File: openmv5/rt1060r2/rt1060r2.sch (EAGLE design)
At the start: 244 parts, among them CN1 S2B-PH-K-S(LF)(SN), IC1 LM66200DRLR, IC2 TCR2LF33,LM_CT, IC3 AP61300Z6-7, IC4 IS42S16160G-6BL, IC5 IS25LP128F-JKLE-TR, IC6 ATECC608B-MAHDA-T, IC7 MXC4005XC, IC8 KSZ8081RNDCA-TR, IC9 MIMXRT1052DVL6B, J1 USB4105-GF-A, J2 USD-1040310811, J3 DF12-36-DS, J4 DNP, J5 DNP, J6 DNP, J7 DNP, J8 3221-10-0300-00, J9 DNP, M1 9774030151R, M2 9774030151R, Q1 DMG2301L-7, Q2 2N7002KW_R1_00001, Q3 2N7002KW_R1_00001, Q4 2N7002KW_R1_00001, Q5 2N7002KW_R1_00001, U1 BQ24075RGTR, U2 LBEE5KL1DX-883, Y1 ECS-327MVATX-3-CN-TR3, Y2 XRCGB24M000F3M00R0, Y3 SC32S-7PF20PPM

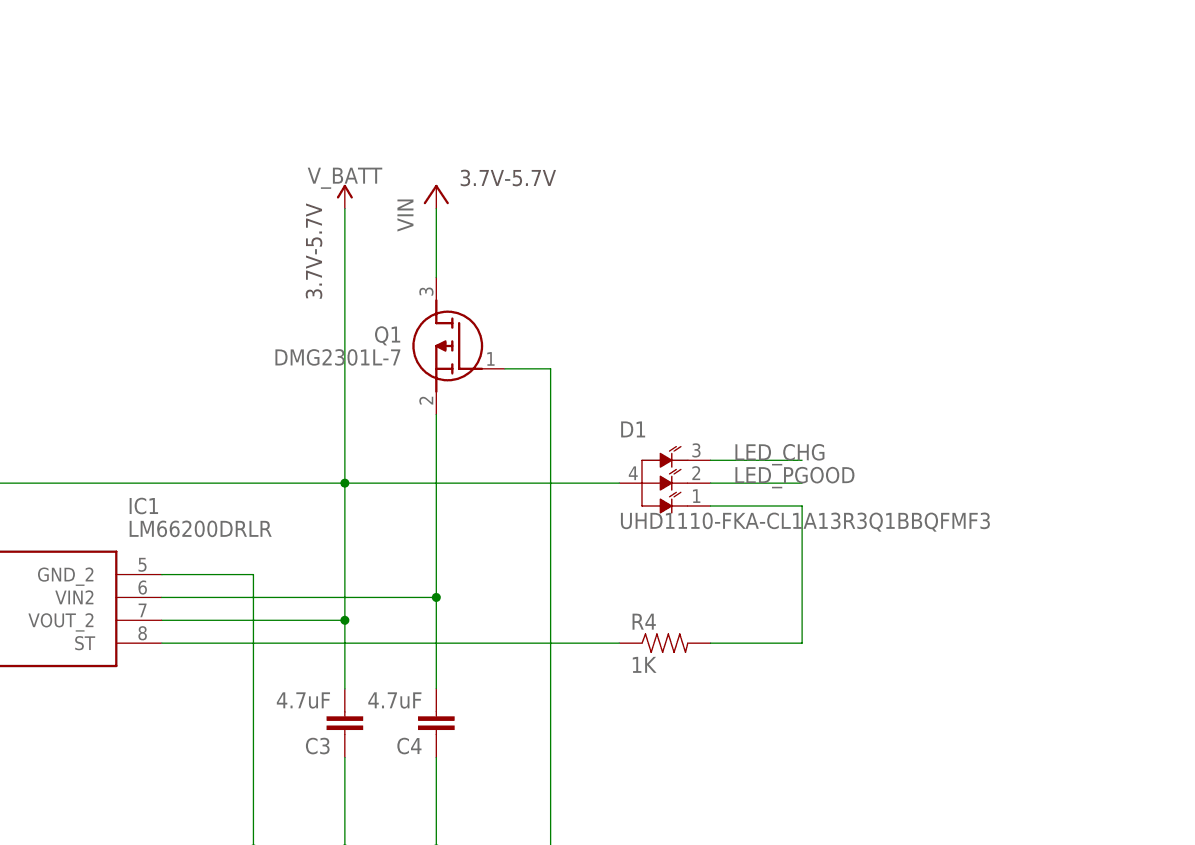
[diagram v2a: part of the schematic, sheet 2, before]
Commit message: Fx leakage issue
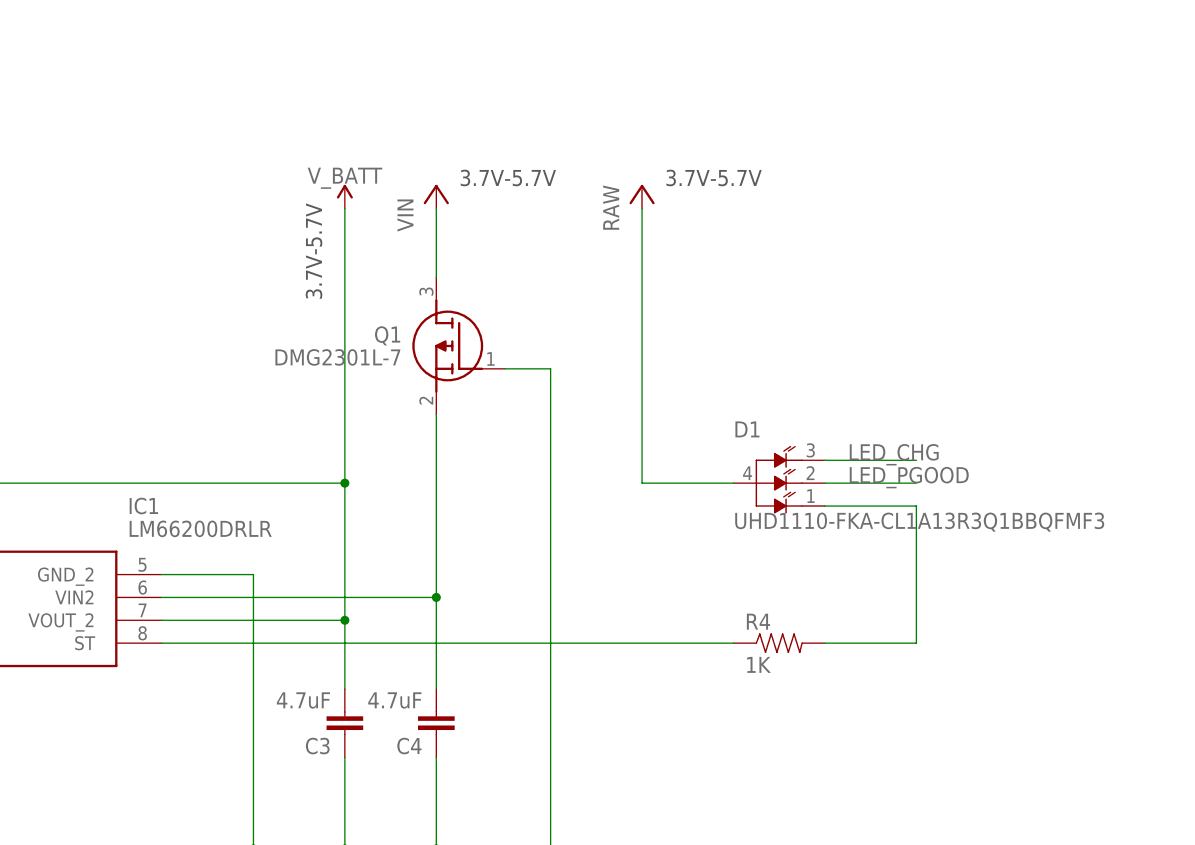
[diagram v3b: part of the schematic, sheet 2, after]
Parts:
- added R63: 10K, 0402:RES_0402
- added R64: 100K, 0402:RES_0402
- R37, R52, R53: value 100K -> 10K; MPN AC0402FR-07100KL -> AC0402FR-1310KL
- R38: value 10K -> 4.7K; MPN AC0402FR-1310KL -> AC0402FR-074K7L
- R40: value 4.7K -> 100K; MPN AC0402FR-074K7L -> AC0402FR-07100KL
- R41, R42: value 10K -> 1K
- R43, R44: value DNP -> 10K; MPN DNP -> AC0402FR-1310KL
- R45: value 100K -> DNP; MPN AC0402FR-07100KL -> DNP
- R46: value 220 -> DNP; MPN CRGCQ0402F220R -> DNP
- R47: value 1K -> 100K; MPN CRCW04021K00FKEDC -> AC0402FR-07100KL
- R48: value 6.49K -> 220; MPN CR0402-FX-6491GLF -> CRGCQ0402F220R
- R50: value 10K -> 6.49K; MPN AC0402FR-1310KL -> CR0402-FX-6491GLF
- R51: value 10K -> 1K; MPN AC0402FR-1310KL -> CRCW04021K00FKEDC
- R57: value 30K -> 100K; MPN 0402WGF3002TCE -> AC0402FR-07100KL
- R59: value 10K -> 30K; MPN AC0402FR-1310KL -> 0402WGF3002TCE
- R60: value 2.2M -> 100K; MPN RC0402FR-072M2L -> AC0402FR-07100KL
- R62: value 10K -> 2.2M; MPN AC0402FR-1310KL -> RC0402FR-072M2L
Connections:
- new net P10_PWM: FL4.INPUT_5, R42.1
- new net PWM_FSIN: IC9.GPIO_SD_B1_01, R40.1, R41.2, R42.2
- net BT_H_WAKE: now also R53.1; no longer R51.1
- net BT_REG_ON: now also R44.1; no longer R42.1
- net DCDC_PSWITCH: now also R59.1; no longer R57.1
- net DCMI_D7: now also R43.1; no longer R41.1
- net DCMI_FSIN: now also R41.1; no longer FL4.INPUT_5, IC9.GPIO_SD_B1_01, R37.1
- net DCMI_PWDN: now also R37.1; no longer R38.1
- net DCMI_SCL: now also R38.1; no longer R39.1
- net DCMI_SDA: now also R39.1; no longer R40.1
- net ETH_INT: now also R49.1; no longer R47.1
- net ETH_LED: now also R48.1; no longer R46.1
- net ETH_MDIO: now also R51.1; no longer R49.1
- net ETH_RST: now also R47.1; no longer R45.1
- net GND: now also R44.2, R50.2, R62.2; no longer R42.2, R48.2, R60.2
- net JTAG_TDI_INT: now also R45.1; no longer R43.1
- net JTAG_TDI_INT_UNUSED: now also R45.2; no longer R43.2
- net JTAG_TRSTB_INT: now also R46.1; no longer R44.1
- net JTAG_TRSTB_INT_UNUSED: now also R46.2; no longer R44.2
- net MDI_LED: now also R48.2; no longer R46.2
- net P12_RST_N: now also R60.2; no longer R58.2
- net PMIC_STBY_REQ: now also R64.1; no longer R62.1
- net RAW: now also D1.ANODE
- net REXT: now also R50.1; no longer R48.1
- net SBL: now also R43.2; no longer R41.2
- net SWITCH: now also R61.1, R63.2; no longer R59.1, R61.2
- net SWITCH_OUT: now also R63.1, R64.2; no longer R61.1, R62.2
- net VCC: now also R58.2, R60.1, R61.2; no longer R45.2, R50.2, R58.1
- net V_BATT: no longer D1.ANODE
- net WIFI_CMD: now also R58.1; no longer R56.1
- net WIFI_D0: now also R57.1; no longer R55.1
- net WIFI_D1: now also R56.1; no longer R54.1
- net WIFI_D2: now also R55.1; no longer R53.1
- net WIFI_D3: now also R54.1; no longer R52.1
- net WL_H_WAKE: now also R52.1; no longer R50.1
- net XTALI: now also R62.1; no longer R60.1
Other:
- moved on the sheet: D1, R37, R38, R39, R4, R40, R44, R47, R48, R49, R52, R53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

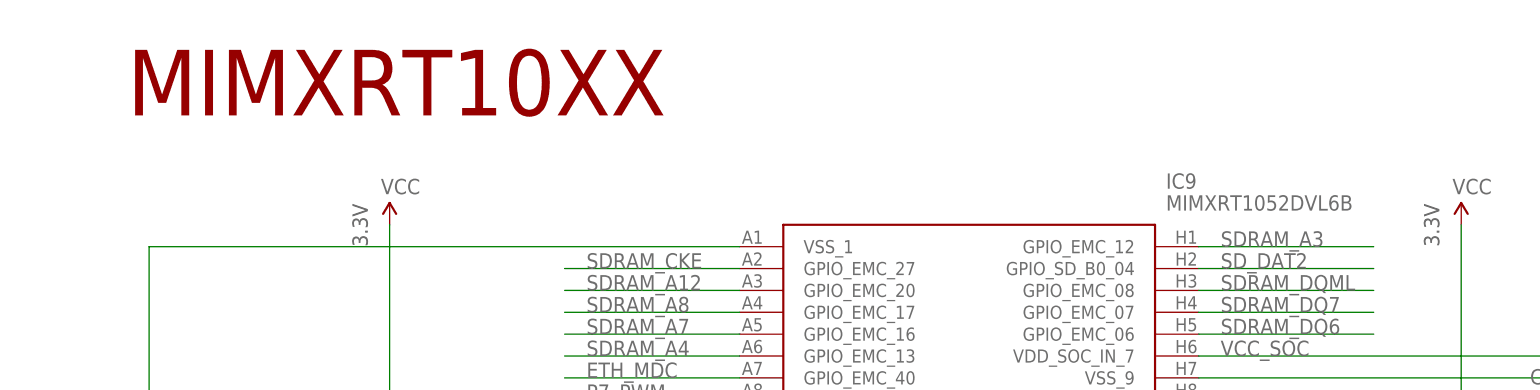
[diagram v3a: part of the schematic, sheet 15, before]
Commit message: Fix processor name
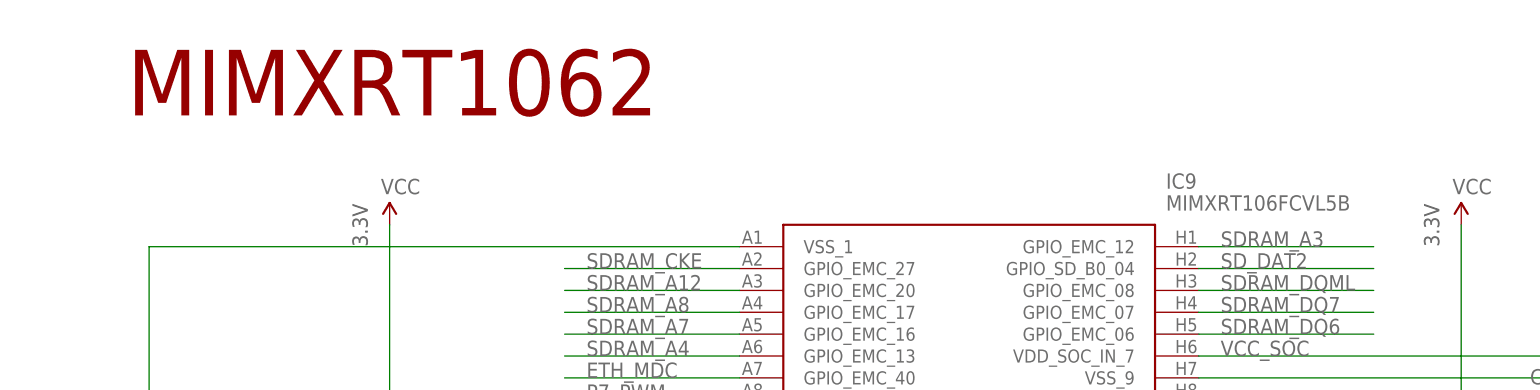
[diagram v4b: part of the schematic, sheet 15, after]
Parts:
- IC9: value MIMXRT1052DVL6B -> MIMXRT106FCVL5B; DESCRIPTION (none) -> Processors - Application Specialized MIMXRT1062DVL6B/LFBGA1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; MANUFACTURER_PART_NUMBER (none) -> MIMXRT1062DVL6B; MOUSER_PART_NUMBER (none) -> 771-MIMXRT1062DVL6B; MOUSER_PRICE-STOCK (none) -> https://www.mouser.co.uk/ProductDetail/NXP-Semiconductors/M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; MPN MIMXRT1052DVL6B -> MIMXRT106FCVL5B
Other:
- note added: "MIMXRT1062"
- note removed: "MIMXRT10XX"
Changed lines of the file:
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@@
 </part>
 <part name="P+1" library="SparkFun" deviceset="VCC" device=""/>
-<part name="IC9" library="MIMXRT1052DVL6B" deviceset="MIMXRT1052DVL6B" device="">
-<attribute name="MPN" value="MIMXRT1052DVL6B"/>
+<part name="IC9" library="MIMXRT1052DVL6B" deviceset="MIMXRT1052DVL6B" device="" value="MIMXRT106FCVL5B">
+<attribute name="DESCRIPTION" value="Processors - Application Specialized MIMXRT1062DVL6B/LFBGA196///STANDARD MARKING * TRAY"/>
+<attribute name="MANUFACTURER_PART_NUMBER" value="MIMXRT1062DVL6B"/>
+<attribute name="MOUSER_PART_NUMBER" value="771-MIMXRT1062DVL6B"/>
+<attribute name="MOUSER_PRICE-STOCK" value="https://www.mouser.co.uk/ProductDetail/NXP-Semiconductors/MIMXRT1062DVL6B"/>
+<attribute name="MPN" value="MIMXRT106FCVL5B"/>
 </part>
 <part name="C32" library="SparkFun-Capacitors" library_urn="urn:adsk.eagle:library:510" deviceset="22UF" device="-0805-6.3V-20%" package3d_urn="urn:adsk.eagle:package:37429/1" value="22uF">
@@
 <text x="2.54" y="2.54" size="2.794" layer="97">To view a copy of this license, visit http://creativecommons.org/licenses/by-sa/3.0/</text>
 <wire x1="0" y1="35.56" x2="165.1" y2="35.56" width="0.1524" layer="94" style="longdash"/>
-<text x="12.7" y="368.3" size="7.62" layer="94" font="vector" ratio="20">MIMXRT10XX</text>
+<text x="12.7" y="368.3" size="7.62" layer="94" font="vector" ratio="20">MIMXRT1062</text>
 <text x="66.04" y="302.26" size="1.778" layer="97">SDRAM_DQS</text>
 <text x="139.7" y="170.18" size="1.778" layer="97">P_FLASH_DQS</text>

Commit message: Fix label issues
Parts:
- C29: value 1uF -> 0.1uF
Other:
- note added: "* CKE is pulled down by 100K on the RT1062"
- note removed: "* CKE is pulled down by 100K on the RT1060"
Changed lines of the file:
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@@
 <attribute name="MPN" value="ATECC608B-MAHDA-T"/>
 </part>
-<part name="C29" library="0402" deviceset="CAP_0402" device="" value="1uF">
+<part name="C29" library="0402" deviceset="CAP_0402" device="" value="0.1uF">
 <spice>
 <pinmapping spiceprefix="C">
@@
 <wire x1="251.46" y1="160.02" x2="149.86" y2="160.02" width="0.1524" layer="150" style="longdash"/>
 <wire x1="149.86" y1="160.02" x2="149.86" y2="167.64" width="0.1524" layer="150" style="longdash"/>
-<text x="152.4" y="162.56" size="2.54" layer="150" font="vector" ratio="20">* CKE is pulled down by 100K on the RT1060</text>
+<text x="152.4" y="162.56" size="2.54" layer="150" font="vector" ratio="20">* CKE is pulled down by 100K on the RT1062</text>
 <text x="40.64" y="142.24" size="1.778" layer="97" rot="R90">3.3V</text>
 <text x="165.1" y="142.24" size="1.778" layer="97" rot="R90">3.3V</text>
